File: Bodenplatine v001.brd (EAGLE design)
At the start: 290 x 145 mm, 113 parts, among them K1 RY612012, K2 RY612012, K3 RY612012, K4 RY612012, K5 RY612012, K6 RY612012, K7 RY612012, K8 RY612012, K9 RY612012, Q1 BC846BLT1SMD, Q2 BC846BLT1SMD, Q3 BC846BLT1SMD, Q4 BC846BLT1SMD, Q5 BC846BLT1SMD, Q6 BC846BLT1SMD, Q7 BC846BLT1SMD, Q8 BC846BLT1SMD, Q9 BC846BLT1SMD, X1 SPRINGCON_AST125_5X2, X10 SPRINGCON_AST125_3X2, X11 SPRINGCON_AST125_4X2, X12 SPRINGCON_AST125_4X2, X13 SPRINGCON_AST125_5X2, X14 236-403, X15 236-402, X2 SPRINGCON_AST125_5X2, X3 SPRINGCON_AST125_5X2, X4 SPRINGCON_AST125_5X2, X5 SPRINGCON_AST125_5X2, X6 SPRINGCON_AST125_5X2, X7 SPRINGCON_AST125_5X2, X8 SPRINGCON_AST125_5X2, X9 SPRINGCON_AST125_5X2

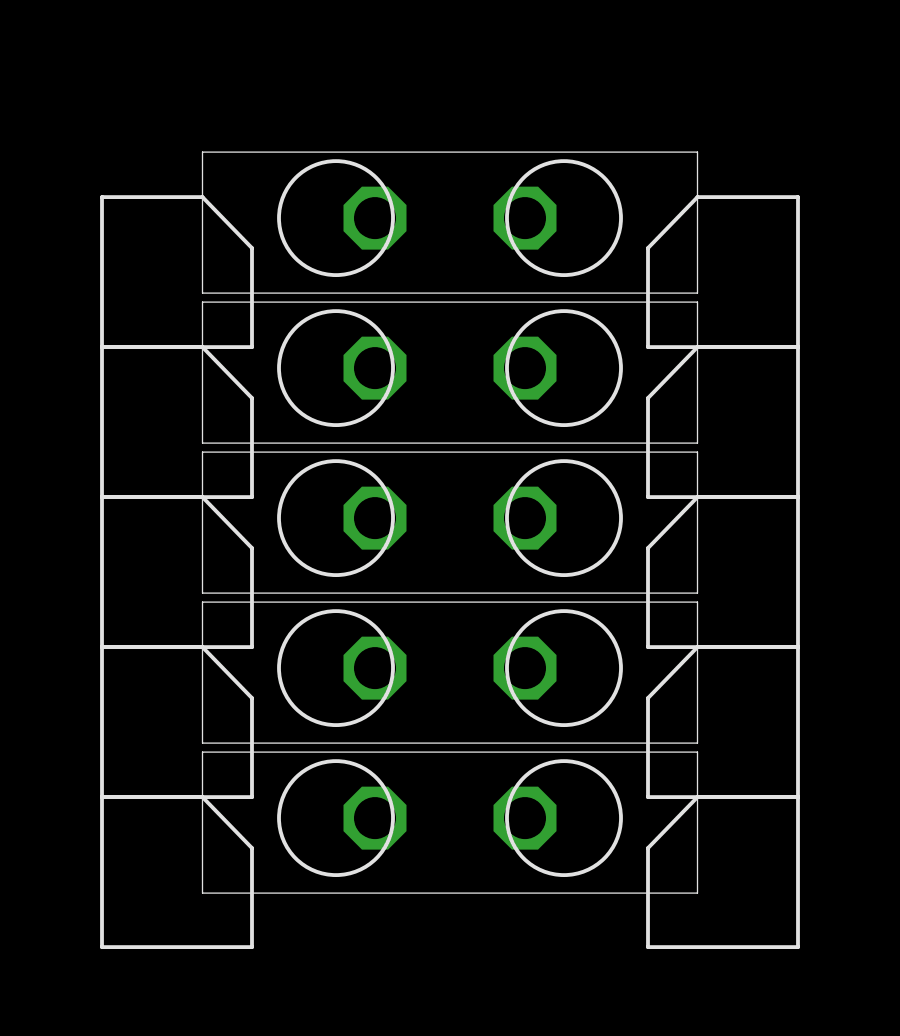
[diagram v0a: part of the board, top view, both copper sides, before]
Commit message: Alle Connectoren mit 2 Pins richtig verbunden.@
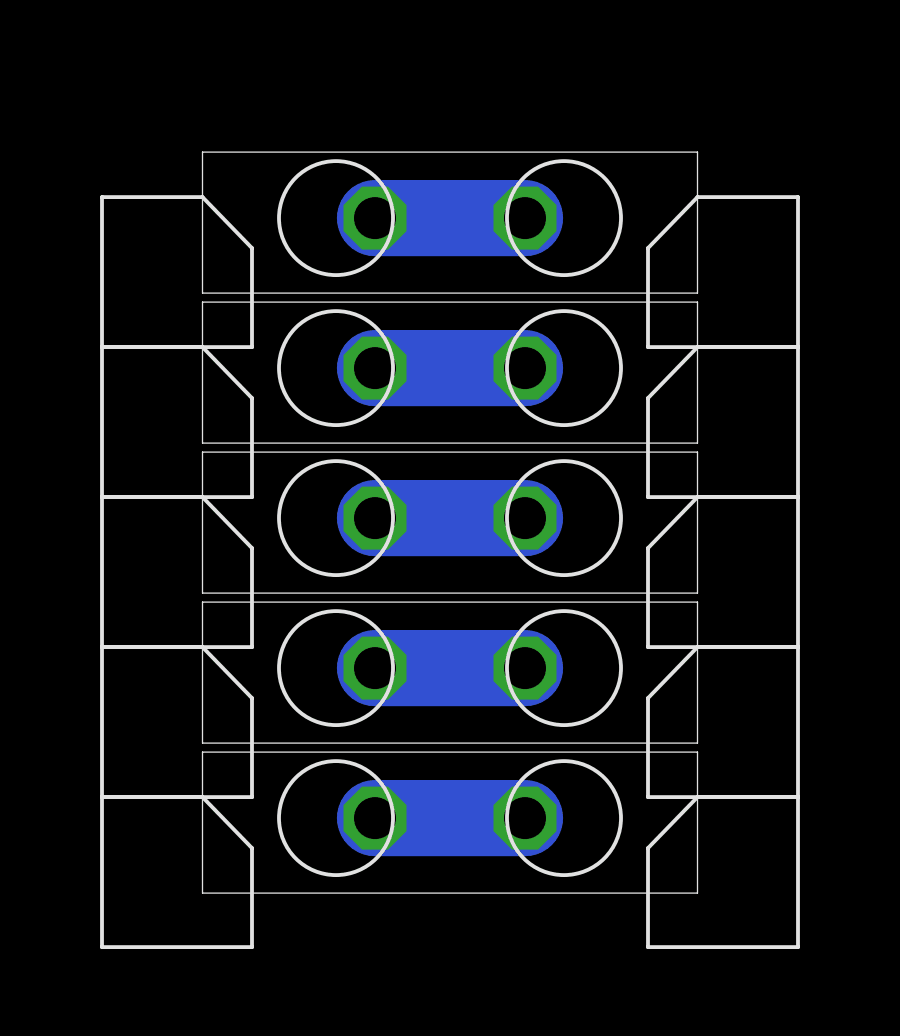
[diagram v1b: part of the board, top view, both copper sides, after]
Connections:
- net B+: now also X13.3'
- net GND: now also X12.3', X12.4', X13.2'
- net L: now also X11.1', X11.2', X11.3', X11.4'
- net N: now also X1.4', X10.2', X2.4', X3.4', X4.4', X5.4', X6.4', X7.4', X8.4', X9.4'
- net N$1: now also X2.2'
- net N$19: now also X3.2'
- net N$2: now also X2.3'
- net N$20: now also X3.1'
- net N$21: now also X4.3'
- net N$29: now also X4.2'
- net N$30: now also X4.1'
- net N$31: now also X5.3'
- net N$39: now also X5.2'
- net N$4: now also X2.1'
- net N$40: now also X5.1'
- net N$41: now also X6.3'
- net N$49: now also X6.2'
- net N$50: now also X6.1'
- net N$51: now also X7.3'
- net N$59: now also X7.2'
- net N$6: now also X3.3'
- net N$60: now also X7.1'
- net N$61: now also X8.3'
- net N$69: now also X8.2'
- net N$70: now also X8.1'
- net N$71: now also X9.3'
- net N$79: now also X9.2'
- net N$80: now also X9.1'
- net N$81: now also X1.3'
- net N$89: now also X1.2'
- net N$90: now also X1.1'
- net N$91: now also X10.1'
- net N$92: now also X13.1'
- net N$94: now also X12.1', X12.2'
- net PE: now also X10.3'
- net SCHIRM: now also X13.5'
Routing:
- net PE: track 0.00 -> 5.00 mm
- net N$90: track 0.00 -> 5.00 mm
- net N$89: track 0.00 -> 5.00 mm
- net N$81: track 0.00 -> 5.00 mm
- net N: track 0.00 -> 5.00 mm

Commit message: Doppelte Kontakte der Connectoren verbunden
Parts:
- moved X14 4.00 mm to (22.0, 130.0)
- moved X15 4.00 mm to (55.0, 130.0)
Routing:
- net PE: track 5.00 -> 50.0 mm
- net N: track 5.00 -> 50.0 mm
- net L: track 0.00 -> 35.0 mm
- net GND: track 0.00 -> 20.0 mm
- net N$94: track 0.00 -> 15.0 mm
- net SCHIRM: track 0.00 -> 5.00 mm
- net N$92: track 0.00 -> 5.00 mm
- net N$91: track 0.00 -> 5.00 mm
- net N$80: track 0.00 -> 5.00 mm
- net N$79: track 0.00 -> 5.00 mm
- net N$71: track 0.00 -> 5.00 mm
- net N$70: track 0.00 -> 5.00 mm
- net N$69: track 0.00 -> 5.00 mm
- net N$61: track 0.00 -> 5.00 mm
- net N$60: track 0.00 -> 5.00 mm
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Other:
- board text added: "0 A 1"
- board text added: "12 Volt Spannungsversorgung BUS"
- board text added: "230 V Netz"
- board text added: "Spannung 12V Netzteil"
- board text added: "Stützklemme 12 Volt"
- board text added: "Stützklemme Phase"
- board text added: "Verbindung zur Deckelplatine"

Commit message: Sicherungshalter nach FPG4 ausgetauscht
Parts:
- F1, F10, F12, F13, F2, F3, F4, F5, F6, F7, F8, F9: device xMZ-Mod-Touch-Bodenplatine:F456 -> xMZ-Mod-Touch-Bodenplatine:FPG4
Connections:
- net 12V: now also F12.1', F13.1'
- net L: now also F10.1'
- net N$1: now also F2.1'
- net N$12: now also F3.2'
- net N$19: now also F3.1'
- net N$22: now also F4.2'
- net N$29: now also F4.1'
- net N$3: now also F2.2'
- net N$32: now also F5.2'
- net N$39: now also F5.1'
- net N$42: now also F6.2'
- net N$49: now also F6.1'
- net N$52: now also F7.2'
- net N$59: now also F7.1'
- net N$62: now also F8.2'
- net N$69: now also F8.1'
- net N$72: now also F9.2'
- net N$79: now also F9.1'
- net N$82: now also F1.2'
- net N$89: now also F1.1'
- net N$91: now also F10.2'
- net N$92: now also F13.2'
- net N$94: now also F12.2'
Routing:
- net GND: track 20.0 -> 0.00 mm
- net N$91: track 5.00 -> 0.00 mm

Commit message: Relais Anschlüsse A1 und A2 im Schema gedreht
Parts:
- moved Q1 17.8 mm to (43.4, 104.3), turned to 180 degrees
- moved R26 14.8 mm to (43.9, 112.0), turned to 180 degrees
- moved R9 12.2 mm to (58.6, 112.1), turned to 270 degrees
- moved X14 10.0 mm to (12.0, 129.5)
- moved R27 9.45 mm to (39.7, 113.9), turned to 180 degrees
- moved R25 7.54 mm to (47.2, 117.5), turned to 90 degrees
- moved Q2 6.34 mm to (60.3, 108.5)
- moved R5 5.59 mm to (34.9, 107.9), turned to 180 degrees
- moved X15 2.83 mm to (53.0, 128.0)
- moved D25 2.08 mm to (41.6, 117.3), turned to 90 degrees
- moved D5 1.12 mm to (35.4, 106.2)
- moved D27 0.47 mm to (34.7, 102.8), turned to 0 degrees
- turned F10 to 0 degrees
- turned F12 to 0 degrees
- turned F13 to 0 degrees
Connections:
- net N$11: now also K2.A1; no longer K2.A2
- net N$17: now also K3.A1; no longer K3.A2
- net N$18: now also K3.A2; no longer K3.A1
- net N$27: now also K4.A1; no longer K4.A2
- net N$28: now also K4.A2; no longer K4.A1
- net N$37: now also K5.A1; no longer K5.A2
- net N$38: now also K5.A2; no longer K5.A1
- net N$47: now also K6.A1; no longer K6.A2
- net N$48: now also K6.A2; no longer K6.A1
- net N$5: now also K2.A2; no longer K2.A1
- net N$57: now also K7.A1; no longer K7.A2
- net N$58: now also K7.A2; no longer K7.A1
- net N$67: now also K8.A1; no longer K8.A2
- net N$68: now also K8.A2; no longer K8.A1
- net N$77: now also K9.A1; no longer K9.A2
- net N$78: now also K9.A2; no longer K9.A1
- net N$87: now also K1.A1; no longer K1.A2
- net N$88: now also K1.A2; no longer K1.A1
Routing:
- net 12V: track 0.00 -> 489.3 mm, vias 0 -> 3
- net GND: track 0.00 -> 361.9 mm, vias 0 -> 1
- net PE: track 50.0 -> 378.7 mm
- net N: track 50.0 -> 367.4 mm
- net A-: track 5.00 -> 269.7 mm
- net B+: track 5.00 -> 267.1 mm
- net 5V: track 0.00 -> 230.0 mm
- net L: track 35.0 -> 247.2 mm
- net N$79: track 5.00 -> 34.7 mm
- net N$69: track 5.00 -> 34.5 mm
- net N$49: track 5.00 -> 34.4 mm
- net N$59: track 5.00 -> 34.4 mm
- net N$19: track 5.00 -> 34.4 mm
- net N$29: track 5.00 -> 34.2 mm
- net N$1: track 5.00 -> 34.2 mm
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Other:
- board text added: "+12V"
- board text added: ">AUTHOR"
- board text added: ">PROJEKTNAME"
- board text added: ">VERSION"
- board text added: "A-"
- board text added: "B+"
- board text added: "BUS"
- board text added: "GND"
- board text added: "L"
- board text added: "N"
- board text added: "PE"
- board text added: "Schirm"
- board text added: "Spannung zu 12V Netzteil"
- board text added: "v"
- board text removed: "Spannung 12V Netzteil"

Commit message: Replace LL4148 Diode
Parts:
- D10, D11, D12, D21, D22, D23, D24, D27, D9: device diode:DO35-7 -> xMZ-Mod-Touch-Bodenplatine:MINIMELF
- moved R5 33.6 mm to (68.0, 114.2)
- moved R7 28.7 mm to (125.9, 112.9)
- moved R8 28.7 mm to (155.0, 112.4)
- moved R6 28.7 mm to (96.9, 113.8)
- moved R17 27.4 mm to (183.0, 112.9)
- moved Q3 17.9 mm to (100.4, 104.5), turned to 180 degrees
- moved Q4 17.7 mm to (130.1, 103.5), turned to 180 degrees
- moved Q9 17.0 mm to (273.9, 103.5), turned to 180 degrees
- moved Q8 14.8 mm to (244.5, 103.6), turned to 180 degrees
- moved Q5 13.8 mm to (156.7, 103.3), turned to 180 degrees
- moved R23 12.6 mm to (242.6, 110.5)
- moved Q7 12.1 mm to (214.8, 102.8), turned to 180 degrees
- moved R15 11.3 mm to (246.8, 116.5), turned to 90 degrees
- moved R16 11.2 mm to (274.8, 117.0), turned to 90 degrees
- moved Q6 11.2 mm to (185.7, 103.0), turned to 180 degrees
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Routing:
- net N$84: track 9.02 -> 0.00 mm
- net N$18: track 5.82 -> 0.00 mm
- net N$17: track 5.82 -> 0.00 mm
- net N$28: track 5.26 -> 0.00 mm
- net N$27: track 5.26 -> 0.00 mm
- net N$38: track 4.81 -> 0.00 mm
- net N$37: track 4.81 -> 0.00 mm
- net N$78: track 4.43 -> 0.00 mm
- net N$77: track 4.43 -> 0.00 mm
- net N$48: track 4.31 -> 0.00 mm
- net N$47: track 4.31 -> 0.00 mm
- net N$58: track 4.26 -> 0.00 mm
- net N$57: track 4.26 -> 0.00 mm

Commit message: BAR43 Diode verbaut und eingebunden
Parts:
- D1, D13, D14, D15, D16, D2, D25, D3, D4: value BAT54 -> BAR43; device diode:SOT23 -> xMZ-Mod-Touch-Bodenplatine:SOT323

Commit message: Prefix übernommen und GND plane im Board layout benannt
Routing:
- added copper zone on layer 1, net GND
- added copper zone on layer 16, net GND
- removed copper zone on layer 1, net N$93
- removed copper zone on layer 16, net N$95
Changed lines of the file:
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@@
 <setting verticaltext="up"/>
 </settings>
-<grid distance="0.5" unitdist="mm" unit="mm" style="lines" multiple="1" display="yes" altdistance="0.1" altunitdist="mm" altunit="mm"/>
+<grid distance="0.05" unitdist="inch" unit="inch" style="lines" multiple="1" display="yes" altdistance="0.005" altunitdist="inch" altunit="inch"/>
 <layers>
 <layer number="1" name="Top" color="4" fill="1" visible="yes" active="yes"/>
@@
 <layer number="23" name="tOrigins" color="15" fill="1" visible="yes" active="yes"/>
 <layer number="24" name="bOrigins" color="15" fill="1" visible="yes" active="yes"/>
-<layer number="25" name="tNames" color="7" fill="1" visible="yes" active="yes"/>
+<layer number="25" name="tNames" color="7" fill="1" visible="no" active="yes"/>
 <layer number="26" name="bNames" color="7" fill="1" visible="no" active="yes"/>
 <layer number="27" name="tValues" color="7" fill="1" visible="no" active="yes"/>
@@
 <layer number="47" name="Measures" color="7" fill="1" visible="no" active="yes"/>
 <layer number="48" name="Document" color="7" fill="1" visible="no" active="yes"/>
-<layer number="49" name="Reference" color="7" fill="1" visible="yes" active="yes"/>
+<layer number="49" name="Reference" color="7" fill="1" visible="no" active="yes"/>
 <layer number="50" name="dxf" color="7" fill="1" visible="no" active="no"/>
 <layer number="51" name="tDocu" color="6" fill="1" visible="yes" active="yes"/>
@@
 <via x="34.96" y="114.5" extent="1-16" drill="0.508"/>
 <wire x1="30.5" y1="114.5" x2="35.56" y2="114.46" width="1.016" layer="16"/>
-<wire x1="120.283" y1="106.99" x2="129.12" y2="104.65" width="0" layer="19" extent="1-1"/>
-<wire x1="121.25" y1="114.46" x2="120.283" y2="106.99" width="0" layer="19" extent="1-1"/>
-<wire x1="55.65" y1="130.9573" x2="55.65" y2="125.9573" width="0" layer="19" extent="1-1"/>
-<wire x1="92.283" y1="107.45" x2="92.5" y2="114.46" width="0" layer="19" extent="1-1"/>
-<wire x1="34.543" y1="107.44" x2="35" y2="114.46" width="0" layer="19" extent="1-1"/>
-<wire x1="39.9" y1="105.42" x2="34.543" y2="107.44" width="0" layer="19" extent="1-1"/>
-<wire x1="62.853" y1="107.44" x2="63.75" y2="114.46" width="0" layer="19" extent="1-1"/>
-<wire x1="69.55" y1="105.92" x2="62.853" y2="107.44" width="0" layer="19" extent="1-1"/>
-<wire x1="99.43" y1="105.65" x2="92.283" y2="107.45" width="0" layer="19" extent="1-1"/>
-<wire x1="149.383" y1="106.95" x2="150" y2="114.46" width="0" layer="19" extent="1-1"/>
-<wire x1="155.77" y1="104.38" x2="149.383" y2="106.95" width="0" layer="19" extent="1-1"/>
-<wire x1="207.383" y1="106.57" x2="207.5" y2="114.46" width="0" layer="19" extent="1-1"/>
-<wire x1="213.88" y1="103.88" x2="207.383" y2="106.57" width="0" layer="19" extent="1-1"/>
-<wire x1="177.883" y1="106.26" x2="178.75" y2="114.46" width="0" layer="19" extent="1-1"/>
-<wire x1="184.73" y1="104.15" x2="177.883" y2="106.26" width="0" layer="19" extent="1-1"/>
-<wire x1="266.407" y1="106.15" x2="265" y2="114.46" width="0" layer="19" extent="1-1"/>
-<wire x1="272.91" y1="104.65" x2="266.407" y2="106.15" width="0" layer="19" extent="1-1"/>
-<wire x1="235.883" y1="105.61" x2="236.25" y2="114.46" width="0" layer="19" extent="1-1"/>
-<wire x1="243.53" y1="104.69" x2="235.883" y2="105.61" width="0" layer="19" extent="1-1"/>
-<wire x1="141.19" y1="133.73" x2="150" y2="114.46" width="0" layer="19" extent="1-1"/>
-<wire x1="141.19" y1="136.27" x2="141.19" y2="133.73" width="0" layer="19" extent="1-1"/>
-<wire x1="242.5" y1="23" x2="243.53" y2="104.69" width="0" layer="19" extent="1-1"/>
+<polygon width="0.254" layer="16" isolate="0.3048">
+<vertex x="0" y="0"/>
+<vertex x="0" y="145"/>
+<vertex x="290" y="145"/>
+<vertex x="290" y="0"/>
+</polygon>
+<polygon width="0.254" layer="1" isolate="0.3048">
+<vertex x="0" y="0"/>
+<vertex x="0" y="145"/>
+<vertex x="290" y="145"/>
+<vertex x="290" y="0"/>
+</polygon>
 </signal>
 <signal name="N$10">
@@
 <wire x1="268.5" y1="72.09" x2="268.81" y2="72.4" width="2.54" layer="16"/>
 </signal>
-<signal name="N$93">
-<polygon width="0.254" layer="1" isolate="0.3048">
-<vertex x="0" y="0"/>
-<vertex x="0" y="145"/>
-<vertex x="290" y="145"/>
-<vertex x="290" y="0"/>
-<vertex x="0" y="0"/>
-</polygon>
-</signal>
-<signal name="N$95">
-<polygon width="0.254" layer="16" isolate="0.3048">
-<vertex x="0" y="0"/>
-<vertex x="0" y="145"/>
-<vertex x="290" y="145"/>
-<vertex x="290" y="0"/>
-</polygon>
-</signal>
 <signal name="N$91">
